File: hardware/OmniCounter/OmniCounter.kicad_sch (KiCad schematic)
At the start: 8 parts, among them SW1 SW_Push_Dual, SW2 SW_Push_Dual, U1 SN74HC595N, U2 DA04-11GWA, U3 SN74HC595N

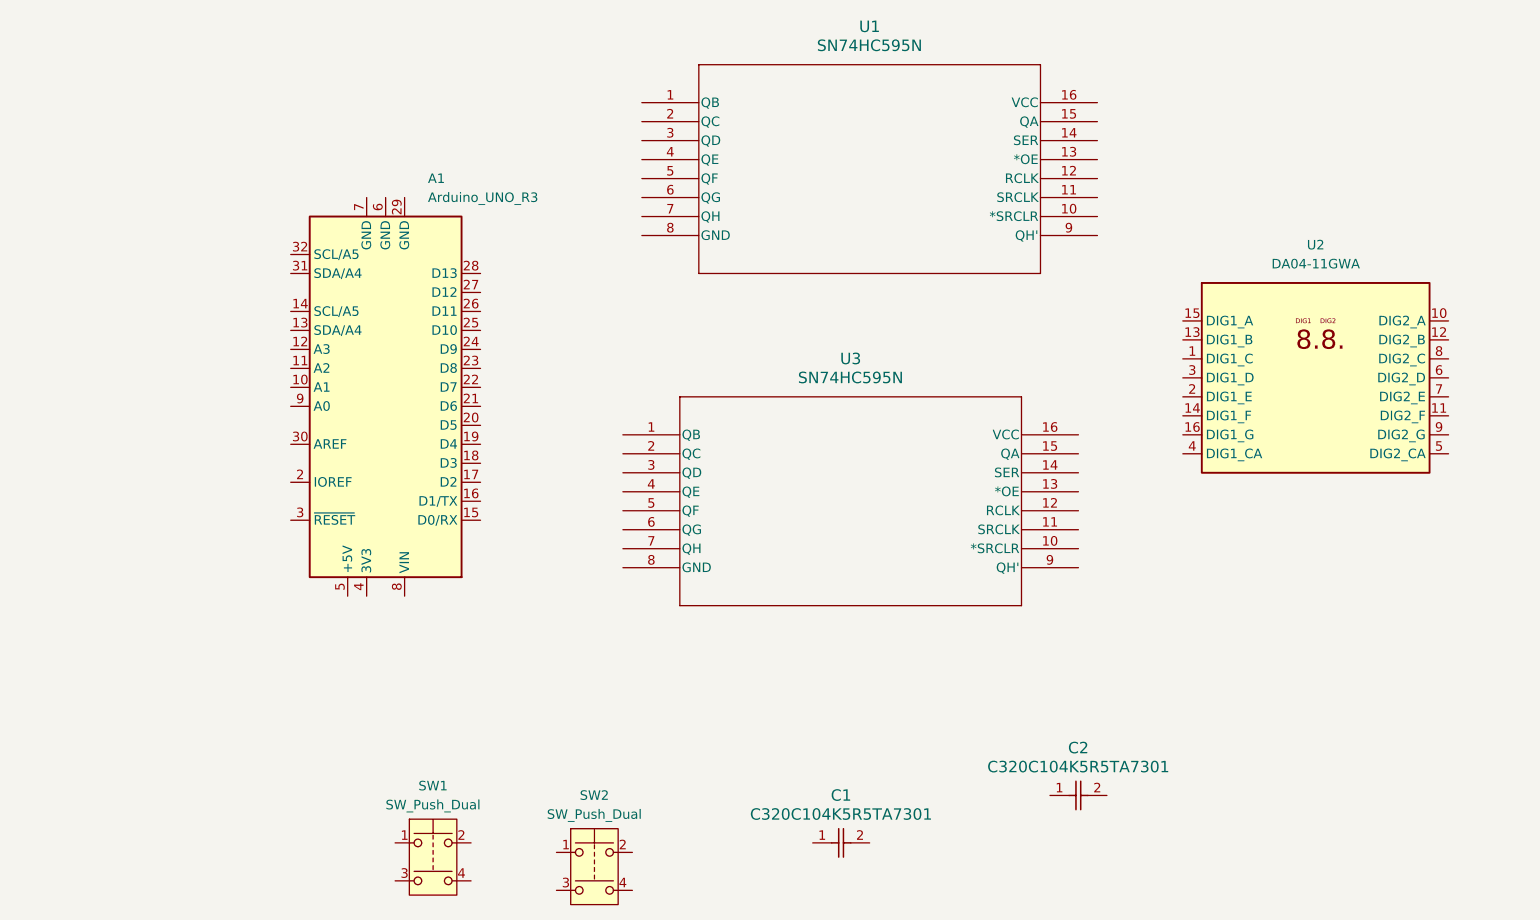
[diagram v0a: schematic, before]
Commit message: Completed Initial Players Counters
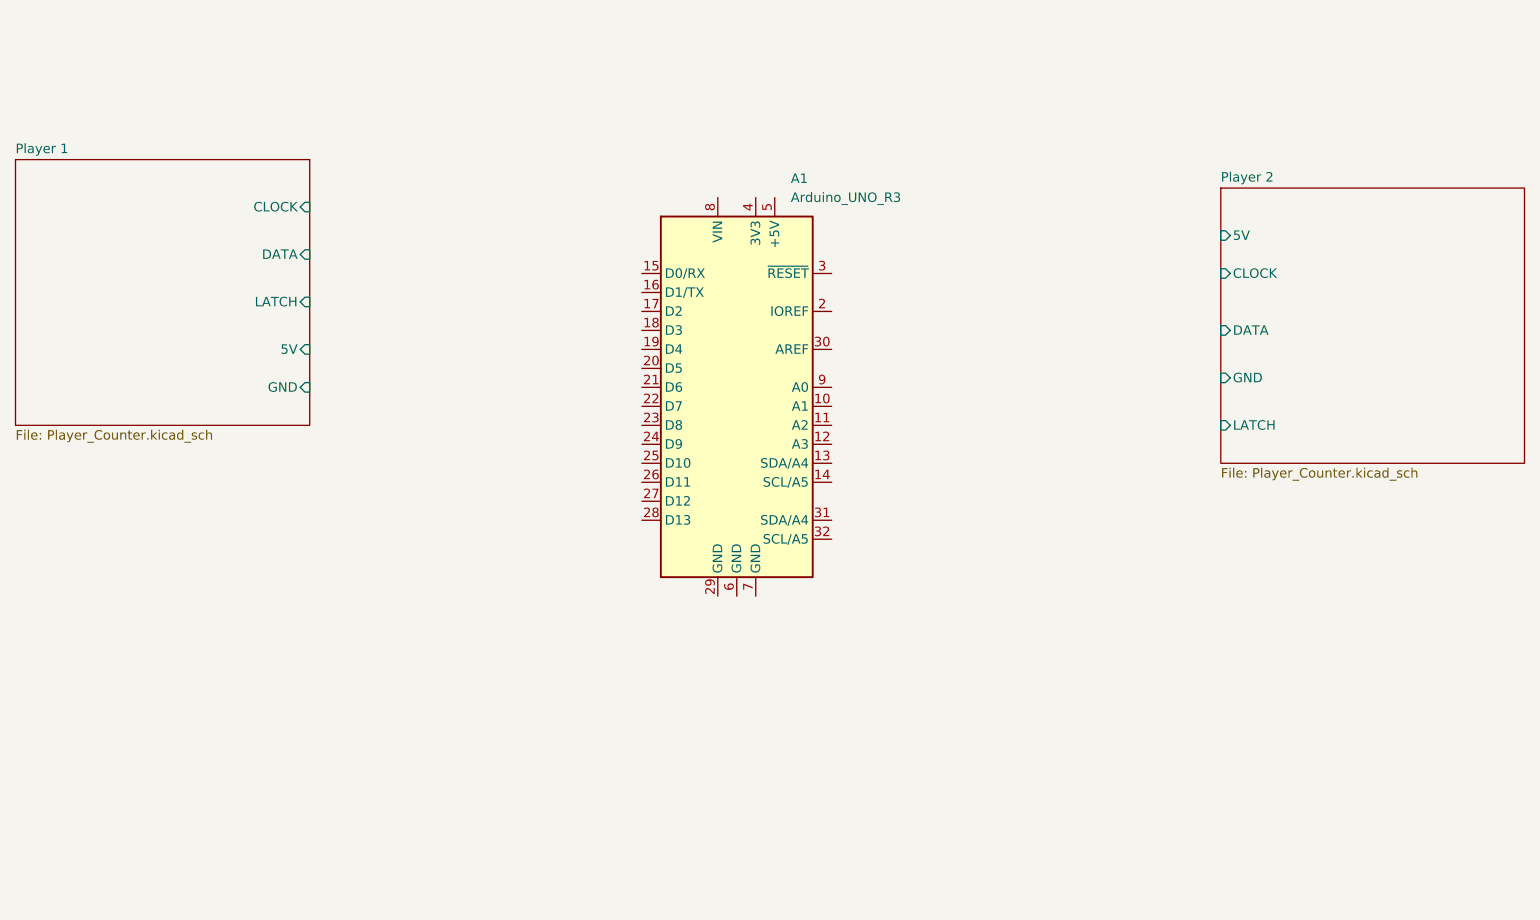
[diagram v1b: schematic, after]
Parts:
- removed C1, C2: C320C104K5R5TA7301, capacitor:CAP_C320C_MR_X7R_KEM, symbol Capacitor:C320C104K5R5TA7301
- removed SW1, SW2: SW_Push_Dual, symbol Switch:SW_Push_Dual
- removed U1, U3: SN74HC595N, SN74HC595N:N16, symbol SN74HC595N:SN74HC595N
- removed U2: DA04-11GWA, Display_7Segment:DA04-11CGKWA, symbol Display_Character:DA04-11GWA
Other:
- added sheet Player 1 (Player_Counter.kicad_sch)
- added sheet Player 2 (Player_Counter.kicad_sch)
- title: 1-Player OmniCounter Schematics -> OmniCounter Schematics
